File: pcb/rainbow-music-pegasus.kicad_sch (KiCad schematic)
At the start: 112 parts, among them J1 USB_B_Micro, J2 Conn_02x03_Odd_Even, J3 B2B-PH-K-S, Q1 DMG3415U, SW1 SW_SPDT, SW2 EVQQ2, U1 ESP32-C3-MINI-1, U2 OPA2322, U3 TLV75533PDBV, U4 MCP73831-2-OT, U5 MCP41050

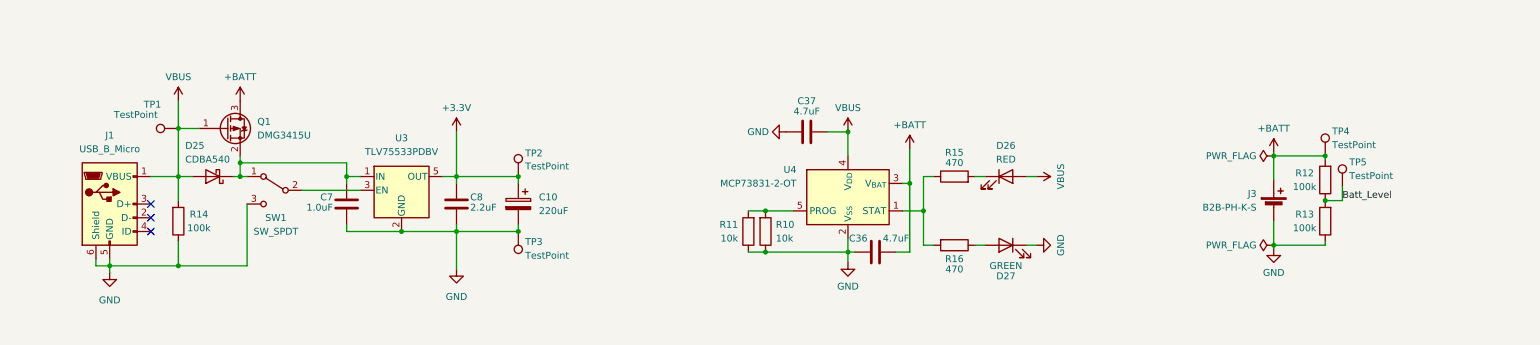
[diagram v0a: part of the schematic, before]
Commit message: Measure the battery level from the Switch common pole
This avoids draining the battery while the power is off, at the cost of
being unable to measure the battery when USB is plugged in.
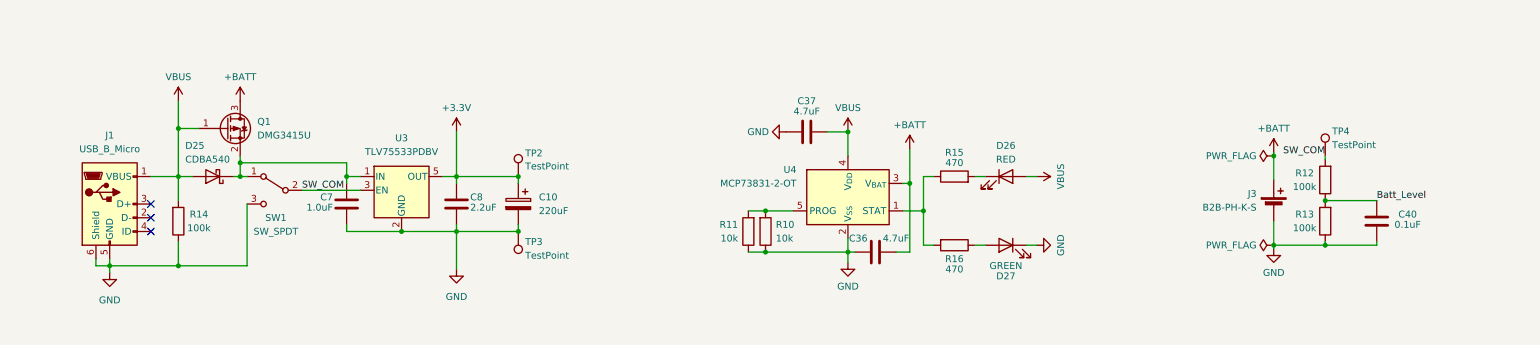
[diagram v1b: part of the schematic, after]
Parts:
- removed TP1, TP5: TestPoint, TestPoint:TestPoint_THTPad_1.5x1.5mm_Drill0.7mm, symbol Connector:TestPoint
- added C40: 0.1uF, Capacitor_SMD:C_0603_1608Metric, symbol Device:C
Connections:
- net +BATT: no longer R12.2, TP4.1
- net Batt_Level: now also C40.1
- net GND: now also C40.2
- net SW_COM: now reaches SW1.2 (B), U3.3 (EN)
- net SW_COM: now also R12.2, TP4.1
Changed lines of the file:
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@@
 	)
 	(junction
+		(at 273.685 161.925)
+		(diameter 0)
+		(color 0 0 0 0)
+	)
+	(junction
 		(at 102.87 159.385)
 		(diameter 0)
@@
 	)
 	(junction
-		(at 273.685 145.415)
-		(diameter 0)
-		(color 0 0 0 0)
-	)
-	(junction
 		(at 303.53 222.25)
 		(diameter 0)
@@
 	(wire
 		(pts
+			(xy 283.21 161.29) (xy 283.21 161.925)
+		)
+		(stroke
+			(width 0)
+			(type default)
+		)
+	)
+	(wire
+		(pts
 			(xy 360.045 226.695) (xy 360.045 227.965)
 		)
@@
 	(wire
 		(pts
-			(xy 273.685 153.67) (xy 276.86 153.67)
+			(xy 273.685 153.67) (xy 283.21 153.67)
 		)
 		(stroke
@@
 	(wire
 		(pts
-			(xy 273.685 145.415) (xy 264.16 145.415)
-		)
-		(stroke
-			(width 0)
-			(type default)
-		)
-	)
-	(wire
-		(pts
 			(xy 360.045 238.125) (xy 353.695 238.125)
 		)
@@
 	(wire
 		(pts
-			(xy 276.86 151.13) (xy 276.86 153.67)
+			(xy 273.685 161.925) (xy 283.21 161.925)
 		)
 		(stroke
@@
 		)
 	)
+	(label "SW_COM"
+		(at 273.685 145.415 180)
+		(effects
+			(font
+				(size 1.27 1.27)
+			)
+			(justify right bottom)
+		)
+	)
 	(label "DP_W"
 		(at 133.35 62.23 180)
@@
 		)
 	)
+	(label "SW_COM"
+		(at 84.455 151.765 0)
+		(effects
+			(font
+				(size 1.27 1.27)
+			)
+			(justify left bottom)
+		)
+	)
 	(label "Reset"
 		(at 362.585 80.01 180)
@@
 	)
 	(label "Batt_Level"
-		(at 276.86 153.67 0)
+		(at 283.21 153.67 0)
 		(effects
 			(font
@@
 	)
 	(symbol
-		(lib_id "Connector:TestPoint")
-		(at 61.595 140.335 90)
-		(mirror x)
-		(unit 1)
-		(body_style 1)
-		(exclude_from_sim no)
-		(in_bom no)
-		(on_board yes)
-		(in_pos_files yes)
-		(dnp no)
-		(property "Reference" "TP1"
-			(at 58.42 135.89 90)
-			(show_name no)
-			(do_not_autoplace no)
-			(effects
-				(font
-					(size 1.27 1.27)
-				)
-				(justify left)
-			)
-		)
-		(property "Value" "TestPoint"
-			(at 57.785 137.795 90)
-			(show_name no)
-			(do_not_autoplace no)
-			(effects
-				(font
-					(size 1.27 1.27)
-				)
-				(justify left)
-			)
-		)
-		(property "Footprint" "TestPoint:TestPoint_THTPad_1.5x1.5mm_Drill0.7mm"
-			(at 61.595 145.415 0)
-			(hide yes)
-			(show_name no)
-			(do_not_autoplace no)
-			(effects
-				(font
-					(size 1.27 1.27)
-				)
-			)
-		)
-		(property "Datasheet" ""
-			(at 61.595 145.415 0)
-			(hide yes)
-			(show_name no)
-			(do_not_autoplace no)
-			(effects
-				(font
-					(size 1.27 1.27)
-				)
-			)
-		)
-		(property "Description" ""
-			(at 61.595 140.335 0)
-			(show_name no)
-			(do_not_autoplace no)
-			(effects
-				(font
-					(size 1.27 1.27)
-				)
-			)
-		)
-		(pin "1"
-		)
-		(instances
-			(project "rainbow-music-pegasus"
-				(path "/4cbaa20b-39f5-487e-a5d4-6b04539cf52b"
-					(reference "TP1")
-					(unit 1)
-				)
-			)
-		)
-	)
-	(symbol
 		(lib_id "power:GND")
 		(at 72.39 85.725 0)
@@
 	)
 	(symbol
-		(lib_id "Connector:TestPoint")
-		(at 276.86 151.13 0)
-		(unit 1)
-		(body_style 1)
-		(exclude_from_sim no)
-		(in_bom no)
-		(on_board yes)
-		(in_pos_files yes)
-		(dnp no)
-		(property "Reference" "TP5"
-			(at 278.13 146.558 0)
-			(show_name no)
-			(do_not_autoplace no)
-			(effects
-				(font
-					(size 1.27 1.27)
-				)
-				(justify left)
-			)
-		)
-		(property "Value" "TestPoint"
-			(at 278.13 149.098 0)
-			(show_name no)
-			(do_not_autoplace no)
-			(effects
-				(font
-					(size 1.27 1.27)
-				)
-				(justify left)
-			)
-		)
-		(property "Footprint" "TestPoint:TestPoint_THTPad_1.5x1.5mm_Drill0.7mm"
-			(at 281.94 151.13 0)
-			(hide yes)
-			(show_name no)
-			(do_not_autoplace no)
-			(effects
-				(font
-					(size 1.27 1.27)
-				)
-			)
-		)
-		(property "Datasheet" ""
-			(at 281.94 151.13 0)
-			(hide yes)
-			(show_name no)
-			(do_not_autoplace no)
-			(effects
-				(font
-					(size 1.27 1.27)
-				)
-			)
-		)
-		(property "Description" ""
-			(at 276.86 151.13 0)
-			(show_name no)
-			(do_not_autoplace no)
-			(effects
-				(font
-					(size 1.27 1.27)
-				)
-			)
-		)
-		(pin "1"
-		)
-		(instances
-			(project "rainbow-music-pegasus"
-				(path "/4cbaa20b-39f5-487e-a5d4-6b04539cf52b"
-					(reference "TP5")
-					(unit 1)
-				)
-			)
-		)
-	)
-	(symbol
 		(lib_id "Device:C_Small")
 		(at 340.995 234.315 0)
@@
 					(unit 1)
 				)
+			)
+		)
+	)
+	(symbol
+		(lib_id "Device:C")
+		(at 283.21 157.48 0)
+		(unit 1)
+		(body_style 1)
+		(exclude_from_sim no)
+		(in_bom yes)
+		(on_board yes)
+		(in_pos_files yes)
+		(dnp no)
+		(property "Reference" "C40"
+			(at 288.925 156.21 0)
+			(show_name no)
+			(do_not_autoplace no)
+			(effects
+				(font
+					(size 1.27 1.27)
+				)
+			)
+		)
+		(property "Value" "0.1uF"
+			(at 288.925 158.115 0)
+			(show_name no)
+			(do_not_autoplace no)
+			(effects
+				(font
+					(size 1.27 1.27)
+				)
+			)
+		)
+		(property "Footprint" "Capacitor_SMD:C_0603_1608Metric"
+			(at 284.1752 161.29 0)
+			(hide yes)
+			(show_name no)
+			(do_not_autoplace no)
+			(effects
+				(font
+					(size 1.27 1.27)
+				)
+			)
+		)
+		(property "Datasheet" ""
+			(at 283.21 157.48 0)
+			(hide yes)
+			(show_name no)
+			(do_not_autoplace no)
+			(effects
+				(font
+					(size 1.27 1.27)
+				)
+			)
+		)
+		(property "Description" ""
+			(at 283.21 157.48 0)
+			(show_name no)
+			(do_not_autoplace no)
+			(effects
+				(font
+					(size 1.27 1.27)
+				)
+			)
+		)
+		(pin "1"
+		)
+		(pin "2"
+		)
+		(instances
+			(project "rainbow-music-pegasus"
+				(path "/4cbaa20b-39f5-487e-a5d4-6b04539cf52b"
+					(reference "C40")
+					(unit 1)
+				)

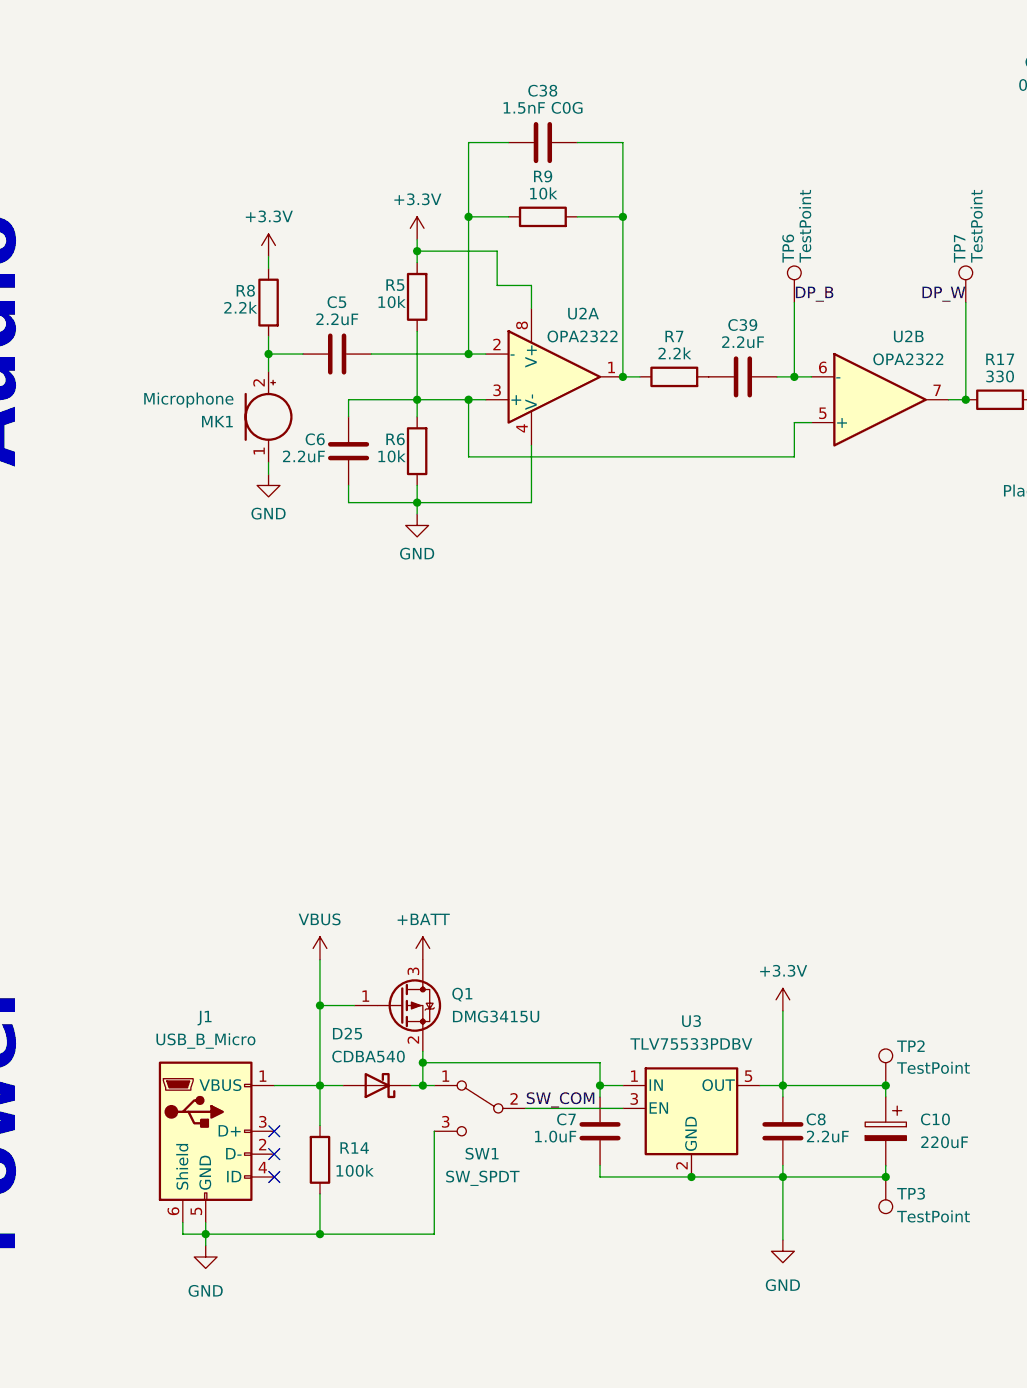
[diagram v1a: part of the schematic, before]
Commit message: Final cleanup of all DRC warnings — added to TODO to upgrade to USB-C
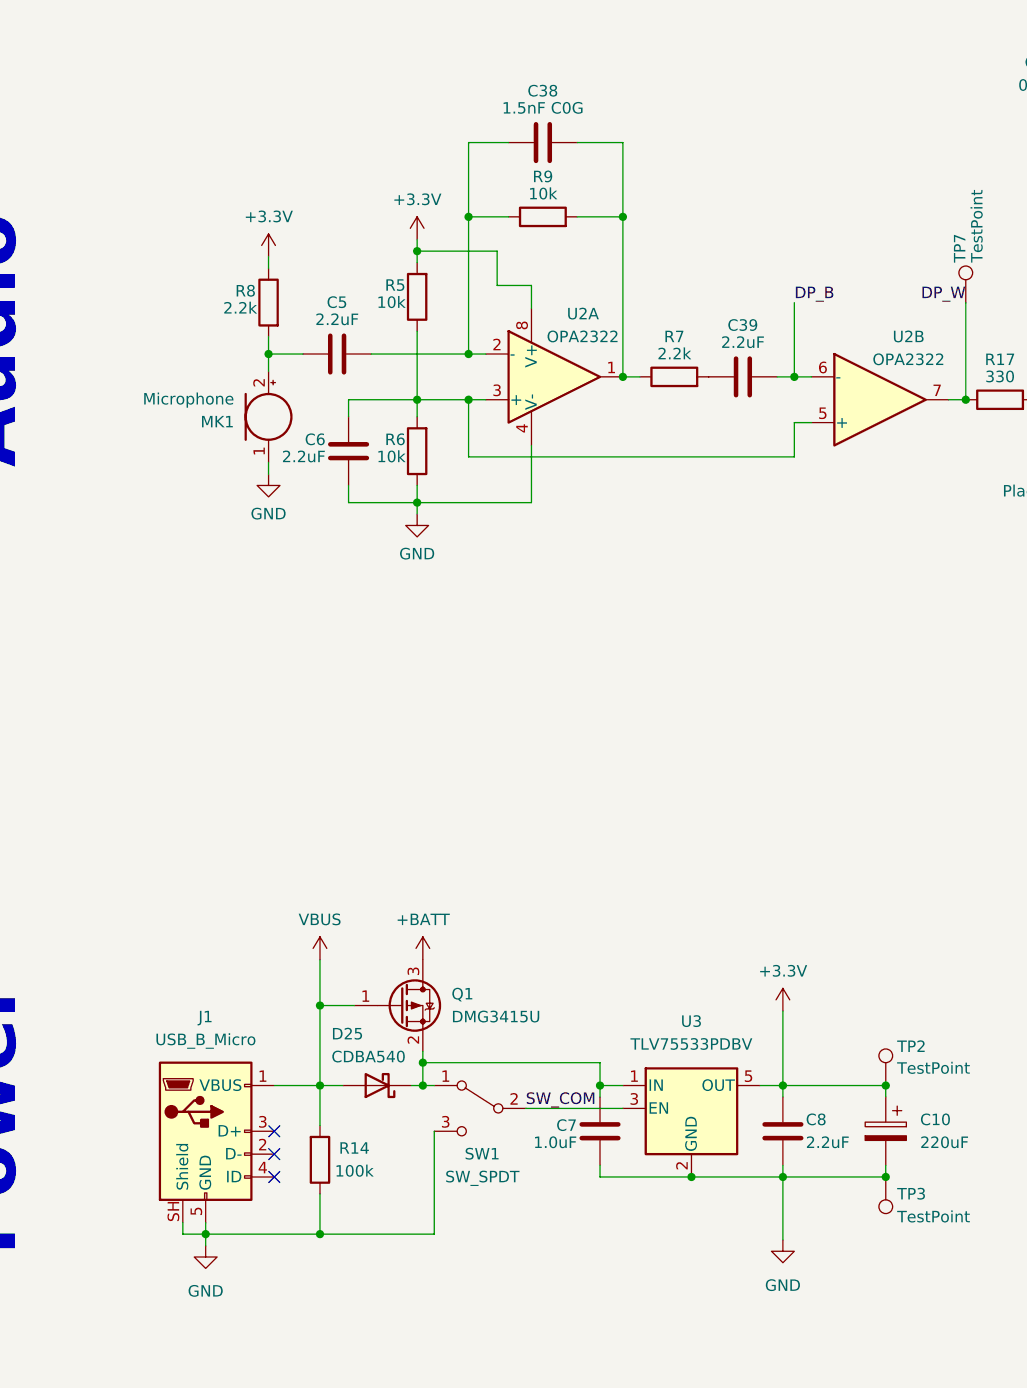
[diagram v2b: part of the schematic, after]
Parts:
- removed TP6: TestPoint, TestPoint:TestPoint_THTPad_1.5x1.5mm_Drill0.7mm, symbol Connector:TestPoint
- SW1: footprint Button_Switch_THT:SW_CuK_OS102011MA1QN1_SPDT_Angled -> Button_Switch_THT:SW_Slide_SPDT_Angled_CK_OS102011MA1Q
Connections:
- net GND: now also J1.SH (Shield); no longer J1.6 (Shield)
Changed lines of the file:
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@@
 		)
 		(property "Value" "2.2uF"
-			(at 115.57 154.94 0)
+			(at 115.57 155.575 0)
 			(show_name no)
 			(do_not_autoplace no)
@@
 	)
 	(symbol
-		(lib_id "Connector:TestPoint")
-		(at 114.3 62.23 0)
-		(mirror y)
-		(unit 1)
-		(body_style 1)
-		(exclude_from_sim no)
-		(in_bom no)
-		(on_board yes)
-		(in_pos_files yes)
-		(dnp no)
-		(property "Reference" "TP6"
-			(at 113.665 57.785 90)
-			(show_name no)
-			(do_not_autoplace no)
-			(effects
-				(font
-					(size 1.27 1.27)
-				)
-				(justify left)
-			)
-		)
-		(property "Value" "TestPoint"
-			(at 115.57 57.785 90)
-			(show_name no)
-			(do_not_autoplace no)
-			(effects
-				(font
-					(size 1.27 1.27)
-				)
-				(justify left)
-			)
-		)
-		(property "Footprint" "TestPoint:TestPoint_THTPad_1.5x1.5mm_Drill0.7mm"
-			(at 109.22 62.23 0)
-			(hide yes)
-			(show_name no)
-			(do_not_autoplace no)
-			(effects
-				(font
-					(size 1.27 1.27)
-				)
-			)
-		)
-		(property "Datasheet" ""
-			(at 109.22 62.23 0)
-			(hide yes)
-			(show_name no)
-			(do_not_autoplace no)
-			(effects
-				(font
-					(size 1.27 1.27)
-				)
-			)
-		)
-		(property "Description" ""
-			(at 114.3 62.23 0)
-			(show_name no)
-			(do_not_autoplace no)
-			(effects
-				(font
-					(size 1.27 1.27)
-				)
-			)
-		)
-		(pin "1"
-		)
-		(instances
-			(project "rainbow-music-pegasus"
-				(path "/4cbaa20b-39f5-487e-a5d4-6b04539cf52b"
-					(reference "TP6")
-					(unit 1)
-				)
-			)
-		)
-	)
-	(symbol
 		(lib_id "power:GND")
 		(at 177.8 264.16 0)
@@
 			)
 		)
-		(property "Description" ""
+		(property "Description" "USB Micro Type B connector"
 			(at 48.895 154.305 0)
+			(hide yes)
 			(show_name no)
 			(do_not_autoplace no)
@@
 		(pin "5"
 		)
-		(pin "6"
+		(pin "SH"
 		)
 		(instances
@@
 		(dnp no)
 		(property "Reference" "C7"
-			(at 90.17 153.035 0)
+			(at 90.17 153.67 0)
 			(show_name no)
 			(do_not_autoplace no)
@@
 		)
 		(property "Value" "1.0uF"
-			(at 90.17 154.94 0)
+			(at 90.17 155.575 0)
 			(show_name no)
 			(do_not_autoplace no)
@@
 			)
 		)
-		(property "Footprint" "Button_Switch_THT:SW_CuK_OS102011MA1QN1_SPDT_Angled"
+		(property "Footprint" "Button_Switch_THT:SW_Slide_SPDT_Angled_CK_OS102011MA1Q"
 			(at 79.375 151.765 0)
 			(hide yes)

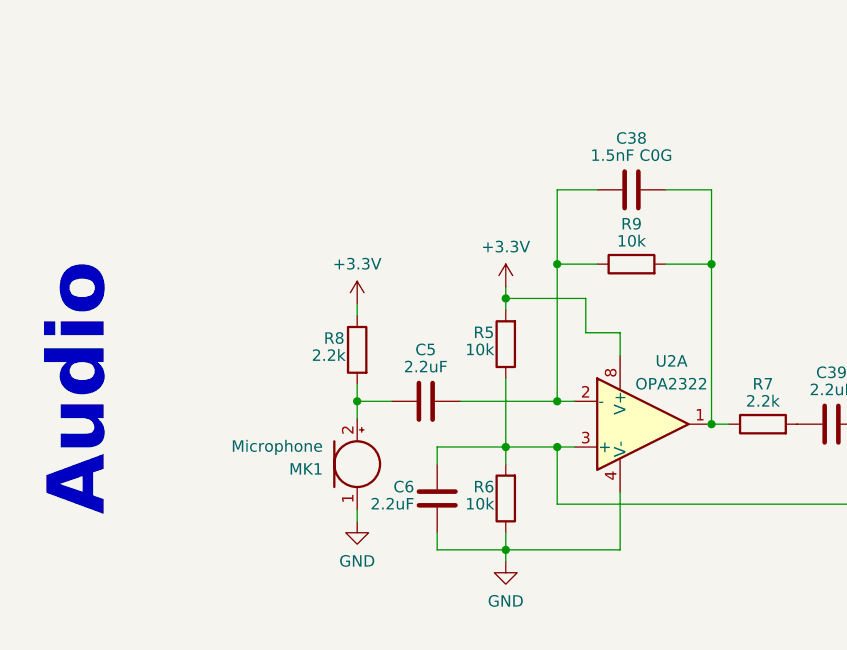
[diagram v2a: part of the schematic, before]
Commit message: Minor correction to R9 and C38 as they were speced using the older v1 mic
Now they're adjusted to support the better AOM-5024P-HD-MB-R microphone.
BOM updated to match, too.
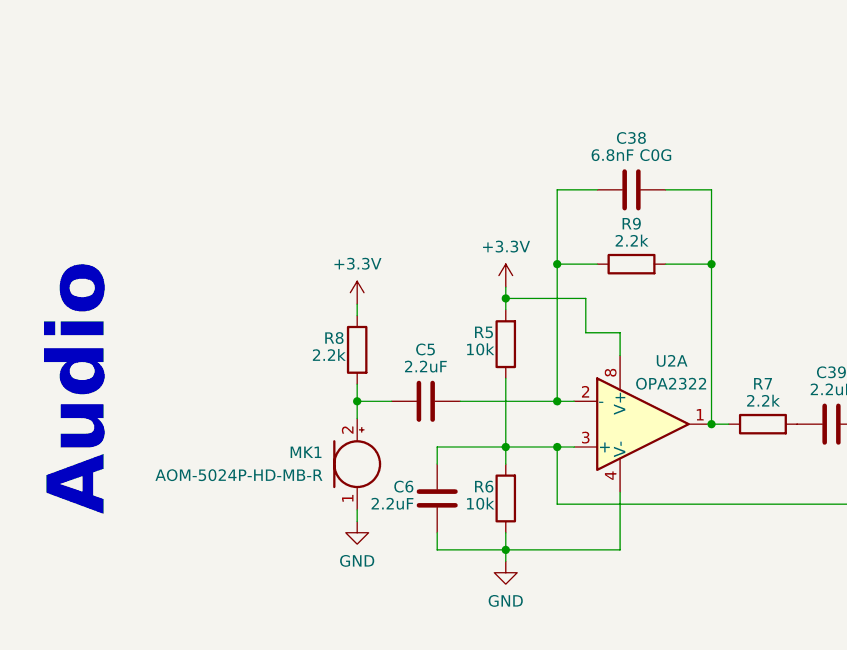
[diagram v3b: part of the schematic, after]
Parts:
- C38: value 1.5nF C0G -> 6.8nF C0G
- MK1: value Microphone -> AOM-5024P-HD-MB-R
- R9: value 10k -> 2.2k
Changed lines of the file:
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@@
 		(dnp no)
 		(property "Reference" "MK1"
-			(at 52.07 75.5015 0)
+			(at 52.07 73.66 0)
 			(show_name no)
 			(do_not_autoplace no)
@@
 			)
 		)
-		(property "Value" "Microphone"
-			(at 52.07 72.9615 0)
+		(property "Value" "AOM-5024P-HD-MB-R"
+			(at 52.07 76.2 0)
 			(show_name no)
 			(do_not_autoplace no)
@@
 			)
 		)
-		(property "Datasheet" ""
+		(property "Datasheet" "https://puiaudio.com/file/specs-AOM-5024P-HD-MB-R.pdf"
 			(at 55.88 72.39 90)
 			(hide yes)
@@
 			)
 		)
-		(property "Value" "1.5nF C0G"
+		(property "Value" "6.8nF C0G"
 			(at 86.36 40.64 90)
 			(show_name no)
@@
 			)
 		)
-		(property "Value" "10k"
+		(property "Value" "2.2k"
 			(at 86.36 50.165 90)
 			(show_name no)

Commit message: Replaced the dual 0603 power status LEDs with a LTST-C195KGJRKT
A little easier to place as the orientation is clear.
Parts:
- removed D26: RED, LED_SMD:LED_0603_1608Metric, symbol Device:LED
- removed D27: GREEN, LED_SMD:LED_0603_1608Metric, symbol Device:LED
- removed TP7: TestPoint, TestPoint:TestPoint_THTPad_1.5x1.5mm_Drill0.7mm, symbol Connector:TestPoint
- added D26: LTST-C195KGJRKT, Altivo:LTST-C195KGJRKT, symbol LED:LTST-C235KGKRKT
- renumbered TP8 to TP1
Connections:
- net GND: now also D26.3 (K2)
- net VBUS: now also D26.2 (A1)
- net at R16.1: now also D26.1 (A2)
- net at R15.2: now also D26.4 (K1)
